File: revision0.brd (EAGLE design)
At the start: 99.5 x 80 mm, 105 parts, among them IC1 MSP430FR698X(1)80-PIN_PN, IC3 FT232RL

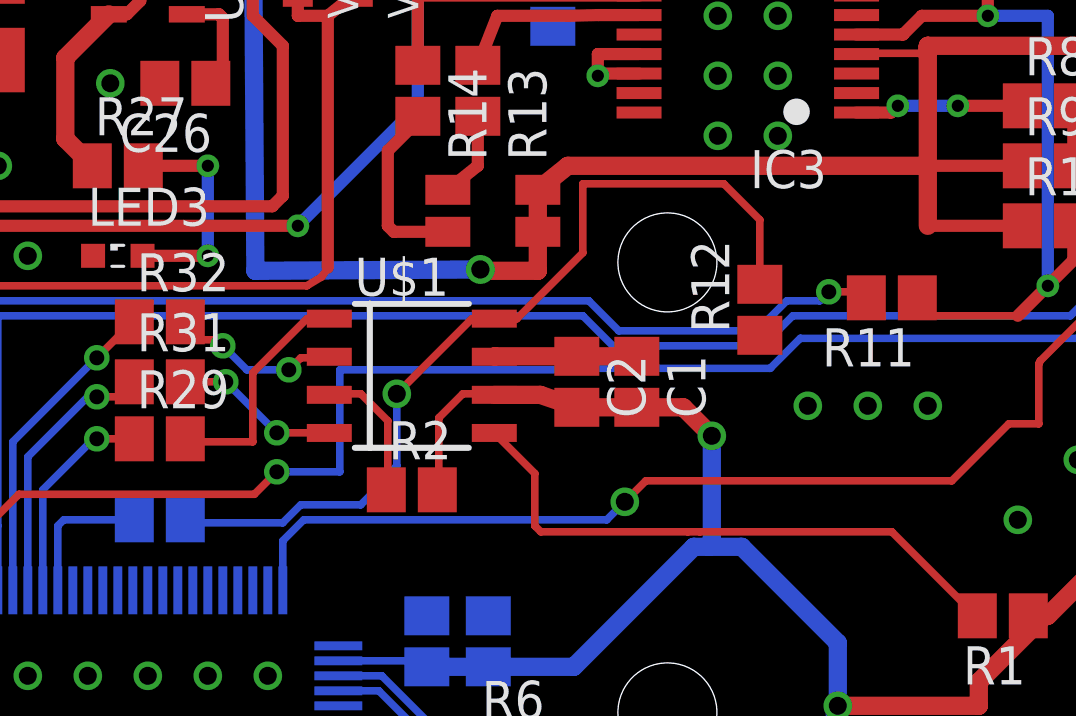
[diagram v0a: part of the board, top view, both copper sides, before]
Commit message: Fix SPI flash package foot print on PCB
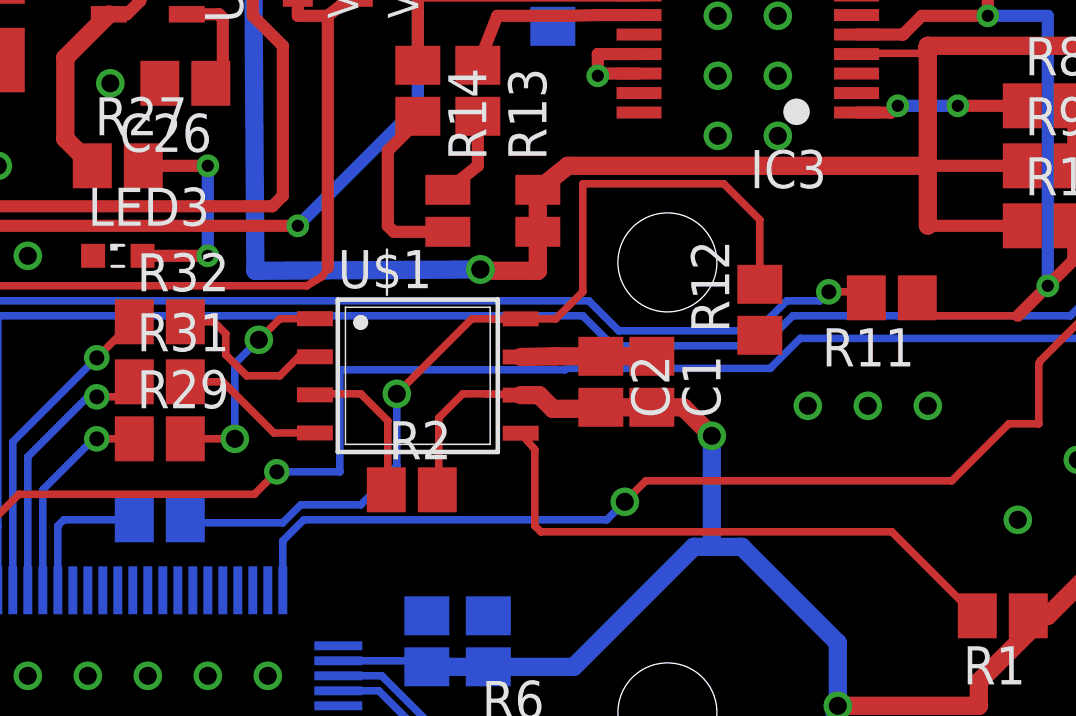
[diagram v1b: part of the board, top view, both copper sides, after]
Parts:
- U$1: value AT45DB641E-SHN -> AT45DB641E-SHNJSOP-08; device tagps:SOIC8 -> tagps:JSOP-08
- moved C2 0.80 mm to (28.1, 60.8)
- moved C1 0.50 mm to (29.8, 60.8)
- moved U$1 0.20 mm to (22.0, 61.0)
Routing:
- net N$14: track 29.5 -> 32.4 mm
- net SPICLK: track 5.93 -> 7.07 mm, vias 2 -> 0
- net SPICSN: track 5.69 -> 5.03 mm, vias 2 -> 0
- net SPISI: track 7.99 -> 7.63 mm, vias 0 -> 2

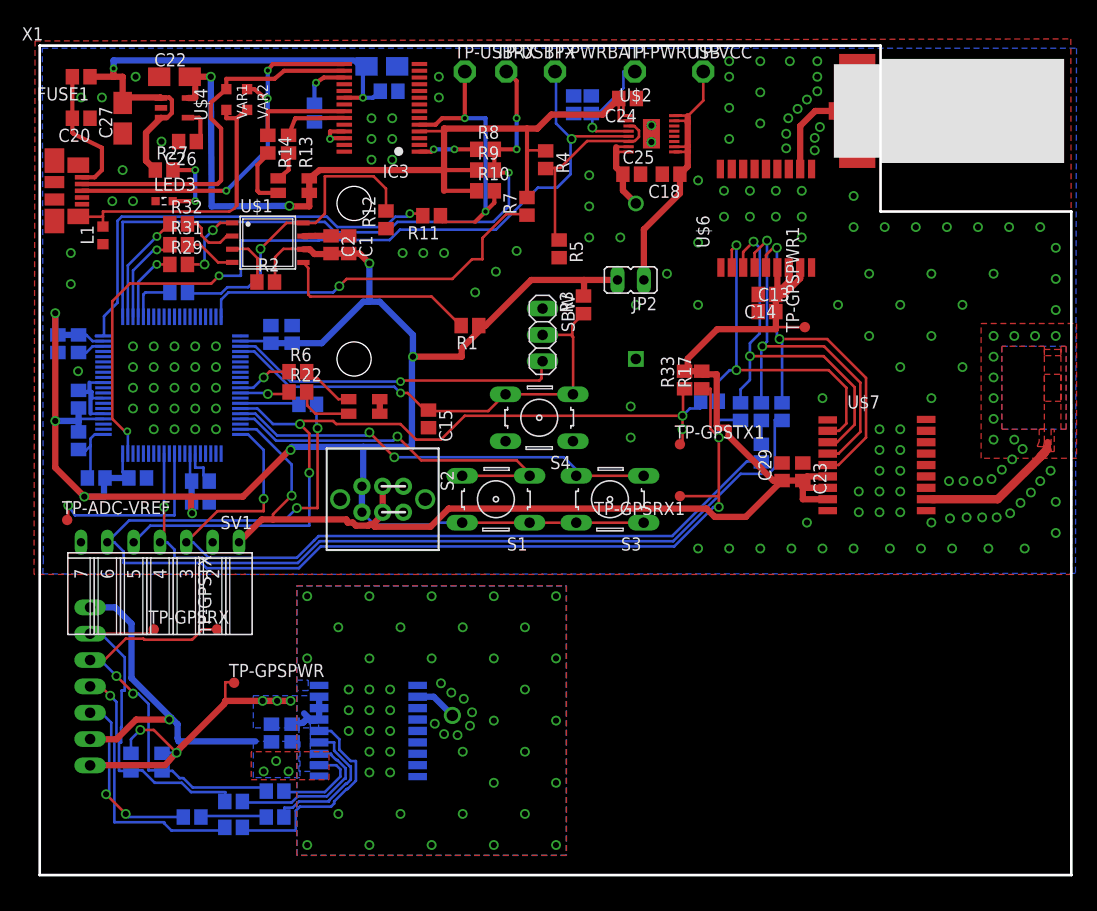
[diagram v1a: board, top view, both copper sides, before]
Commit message: Resize Cc and Rs from 0805->0603
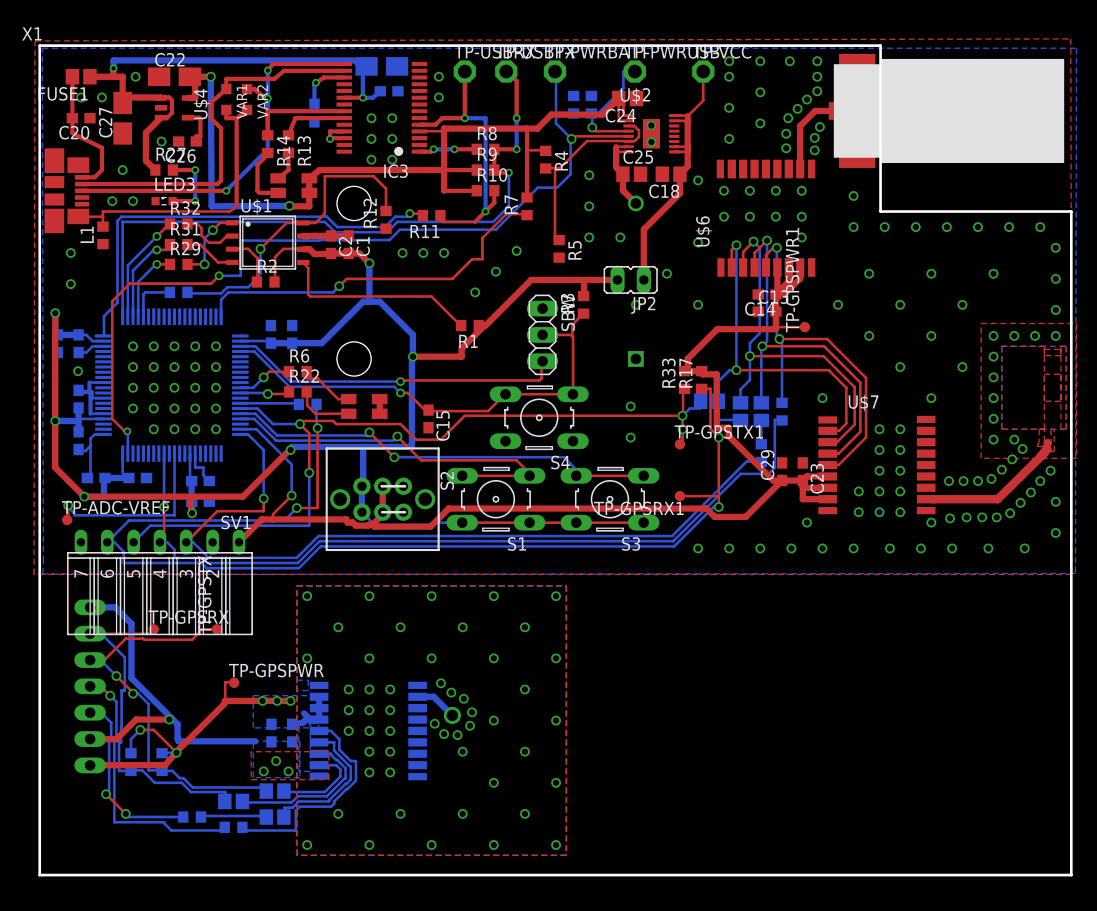
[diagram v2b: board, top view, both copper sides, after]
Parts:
- C1, C10, C11, C12, C13, C14, C15, C16, C17, C19, C2, C20, C21, C23, C26, C29, C3, C4, C5, C6, C7, C8, C9: device tagps:C0805 -> tagps:C0603
- R1, R10, R11, R12, R13, R14, R15, R16, R17, R2, R22, R23, R24, R25, R26, R27, R28, R29, R3, R30, R31, R32, R33, R34, R35, R4, R5, R6, R7, R8, R9: device tagps:R0805 -> tagps:R0603

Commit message: Split board to 2 pieces, remove ADC battery input (was senseless)
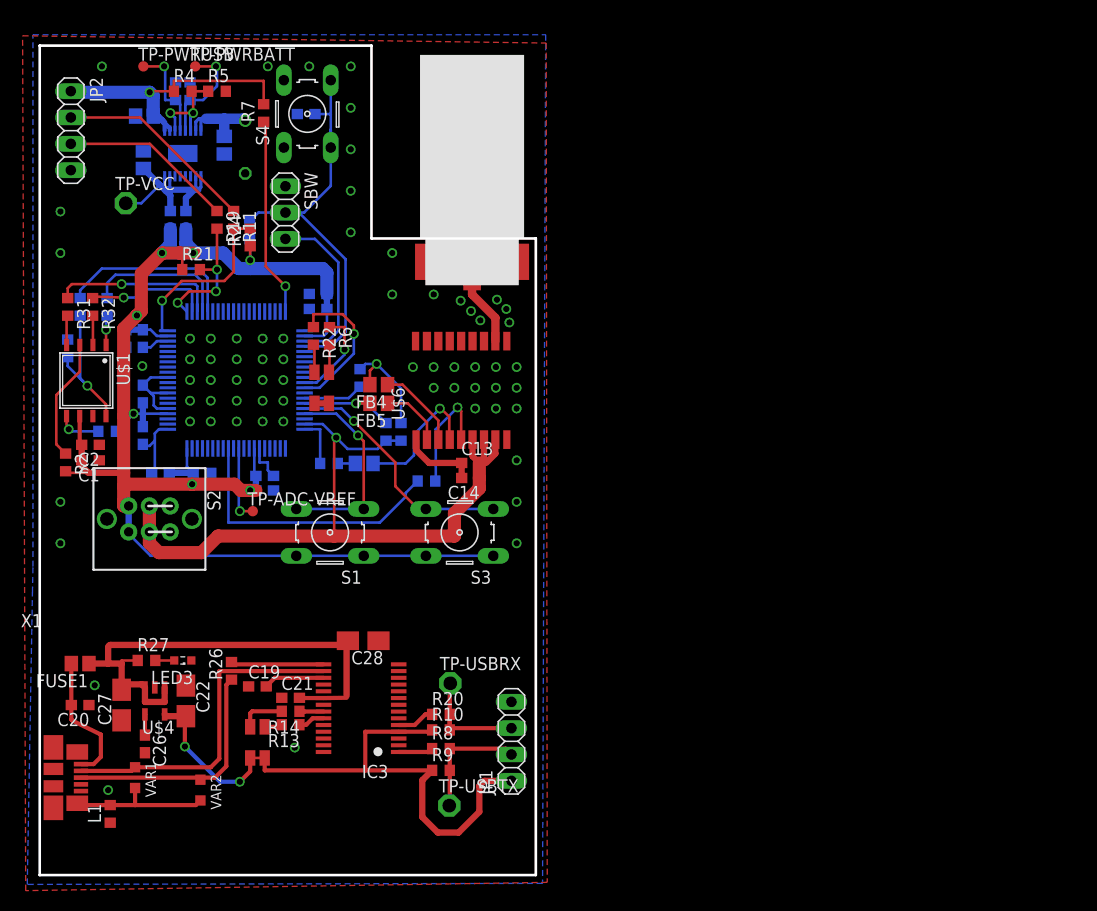
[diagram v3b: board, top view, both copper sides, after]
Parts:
- removed C16, C23: 100n, tagps:C0603
- removed C17, C29: 1u, tagps:C0603
- removed FB1, FB2, FB3: 0, tagps:R0805
- removed R28: 0, tagps:R0603
- removed SV1: (no value), tagps:FE07W
- removed TP-GPSPWR, TP-GPSPWR1, TP-GPSRX, TP-GPSRX1, TP-GPSTX, TP-GPSTX1: TPSQTP10R, tagps:TP10R
- removed TP1: TPSQTP16R, tagps:TP16R
- removed U$3, U$7: MAX-8C-0, tagps:MAX-8
- added R18: 0, tagps:R0603
- added R19, R20: 100, tagps:R0603
- added R21: 33k, tagps:R0603
- G2: value BATTERY -> BATTERYTAP5-45; device tagps:BATHOLD2AA -> tagps:TAP5-45
- JP1: device tagps:1X07/90 -> tagps:1X04
- JP2: device tagps:JP1 -> tagps:1X04
- R24: value 100k -> 33k
- R25: value 100k -> 0
- TP-PWRBATT, TP-PWRUSB: value TPSQPAD1-13 -> TPSQTP10R; device tagps:P1-13 -> tagps:TP10R
- moved TP-USBTX 71.0 mm to (39.5, 6.70)
- moved VAR2 66.8 mm to (15.5, 8.20)
- moved VAR1 66.0 mm to (9.20, 9.40)
- moved C22 60.2 mm to (14.1, 16.8), turned to 270 degrees
- moved C21 59.3 mm to (24.2, 17.1), flipped to the top
- moved TP-USBRX 59.0 mm to (39.6, 18.5)
- moved C26 58.2 mm to (10.2, 12.7), turned to 270 degrees
- moved R9 58.1 mm to (38.7, 10.1)
- moved R8 58.0 mm to (38.7, 12.2)
- moved IC3 57.9 mm to (31.0, 16.1)
- moved U$4 57.2 mm to (11.1, 16.8), turned to 180 degrees
- moved TP-VCC 57.1 mm to (8.30, 64.8)
- moved C20 56.6 mm to (3.90, 16.4)
- moved C27 56.6 mm to (7.90, 16.4)
- moved FUSE1 56.6 mm to (3.90, 20.4)
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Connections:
- removed net ANTENNA: TP1.TP, U$3.11
- removed net GPS-RX: FB1.2, JP1.2, R24.1, TP-GPSRX.TP
- removed net GPS-TIMEPULSE: JP1.5, R28.1
- removed net GPS-TX: FB2.2, JP1.3, R25.1, TP-GPSTX.TP
- removed net GPS-WAKEUP: JP1.4, R26.1
- removed net N$21: FB3.1, U$3.4
- removed net N$50: FB6.1, U$6.4, U$7.4
- removed net N$51: FB2.1, U$3.2
- removed net N$52: FB1.1, U$3.3
- removed net N$9: FB3.2, R28.2
- removed net PWR_GPS_SENSE: C16.2, C17.1, JP1.7, R24.2, R25.2, TP-GPSPWR.TP, U$3.6, U$3.7, U$3.8
- new net FT232-RX: JP1.3, R10.2, R20.2, TP-USBRX.TP
- new net FT232-TX: JP1.2, R8.2, R9.2, TP-USBTX.TP
- new net N$29: IC3.15, R26.2
- new net N$4: IC3.5, R20.1
- new net N$60: FB6.1, U$6.4
- new net VCCUSBGPS: C24.2, JP2.1, R4.1, R7.2, U$2.1, U$2.2
- net ADC-BATT: no longer IC1.59
- net GND: now also JP1.4, JP2.4; no longer C16.1, C17.2, C23.1, C29.2, JP1.1, JP1.6, SV1.2, SV1.7, U$3.1, U$3.10, U$3.12, U$7.1, U$7.10, U$7.12
- net MB-GPS-RX: no longer SV1.6, TP-GPSRX1.TP
- net MB-GPS-TIMEPULSE: no longer SV1.3
- net MB-GPS-TX: no longer SV1.5, TP-GPSTX1.TP
- net MB-GPS-WAKEUP: no longer SV1.4
- net MB-PWR_GPS_SENSE: no longer C23.2, C29.1, SV1.1, TP-GPSPWR1.TP, U$7.6, U$7.7, U$7.8
- net MCU-RX-FT232: now also R19.2, R21.2; no longer R8.2, R9.2, TP-USBTX.TP
- net MCU-TX-FT232: now also JP2.2; no longer IC3.5, R10.2, TP-USBRX.TP
- net N$12: now also R26.1; no longer IC3.15
- net N$15: no longer U$7.3
- net N$2: now also R24.2
- net N$26: now also R18.1, R25.1; no longer JP2.1
- net N$46: no longer U$7.5
- net N$49: no longer U$7.2
- net N$8: now also JP2.3, R19.1; no longer R26.2, U$3.5
- net VCC: now also R18.2, R21.1, R24.1, R25.2; no longer JP2.2
- net VCCUSB: now also JP1.1; no longer C24.2, R4.1, R7.2, U$2.1, U$2.2
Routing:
- net MB-GPS-RX: track 115.0 -> 10.7 mm, vias 4 -> 1
- net ADC-BATT: track 84.7 -> 10.2 mm, vias 3 -> 1
- net MB-GPS-TIMEPULSE: track 77.5 -> 4.80 mm, vias 1 -> 0
- net MB-GPS-TX: track 81.8 -> 9.99 mm, vias 4 -> 1
- net MB-PWR_GPS_SENSE: track 129.3 -> 70.5 mm
- net MCU-RX-FT232: track 64.9 -> 13.2 mm
- net MB-GPS-WAKEUP: track 78.5 -> 27.3 mm, vias 1 -> 0
- net GPS-TX: track 39.9 -> 0.00 mm, vias 2 -> 0
- net N$50: track 38.6 -> 0.00 mm, vias 2 -> 0
- net PWR_GPS_SENSE: track 38.3 -> 0.00 mm, vias 5 -> 0
- net GND: track 66.6 -> 30.5 mm, vias 221 -> 66
- net VCC: track 190.4 -> 155.7 mm
- net GPS-RX: track 34.2 -> 0.00 mm
- net N$15: track 37.7 -> 8.18 mm, vias 2 -> 0
- net N$49: track 35.4 -> 6.22 mm, vias 2 -> 0
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- removed copper zone on layer 1, net N$20
- removed copper zone on layer 1, net N$28
- removed copper zone on layer 16, net N$28
- removed copper zone on layer 1, net N$29
- removed copper zone on layer 1, net N$30
- removed copper zone on layer 16, net N$4
- removed copper zone on layer 16, net PWR_GPS_SENSE
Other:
- board size 99.5 x 80 mm -> 47.9 x 80 mm
- board text added: "PWRBATT"
- board text added: "PWRUSB"
- board text added: "taGPS v3a"
- board text removed: "BATT-PWR-USB"
- board text removed: "GPS-PWR"
- board text removed: "RX-GPS-TX"
- board text removed: "TIMEPULSE"
- board text removed: "taGPS v2 - antenna test"

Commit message: Remove UART pullups and button to make it even smaller
Removed GPS and USB pullups (do not forget to add them
to the MCU IOs!), removed one button, removed unnecesary
GPS ferrite beads
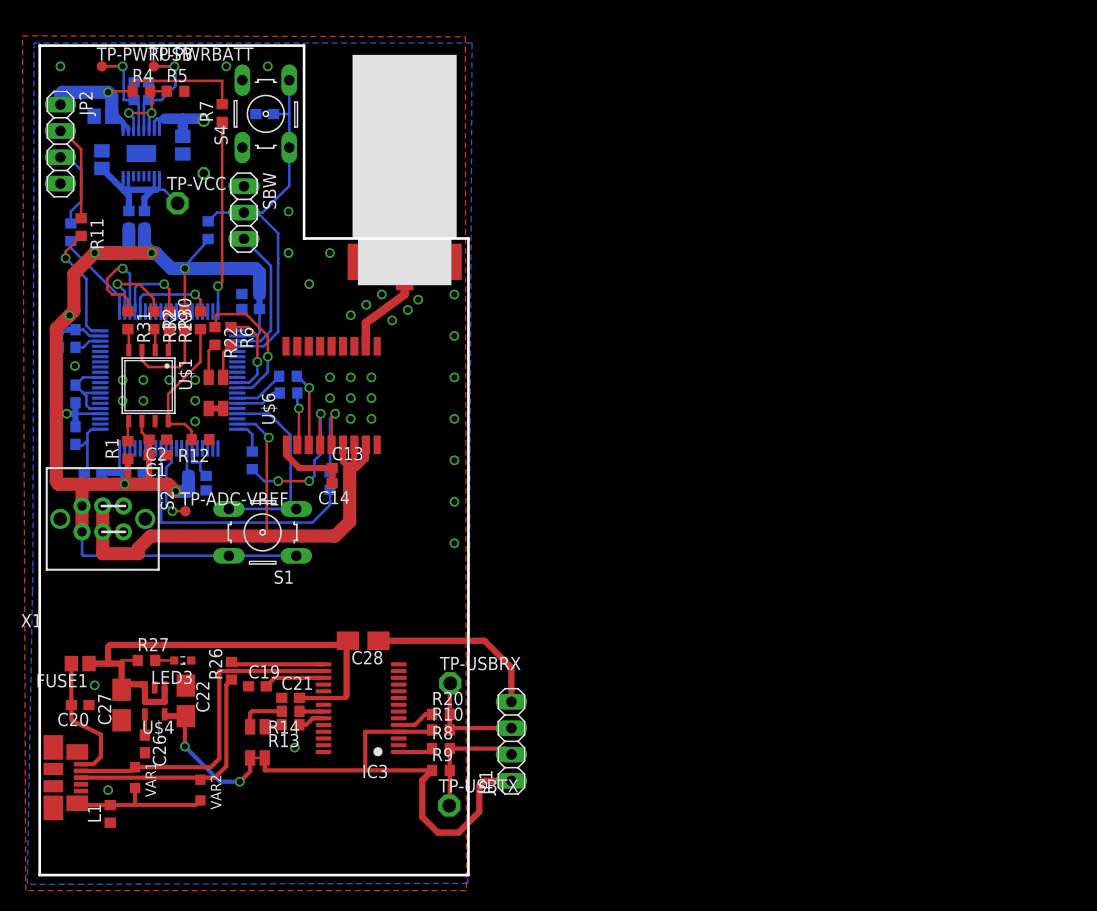
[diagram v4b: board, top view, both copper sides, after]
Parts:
- removed FB4, FB5, FB6: 0, tagps:R0805
- removed R17, R33: 100k, tagps:R0603
- removed R21, R24: 33k, tagps:R0603
- removed S3: (no value), tagps:B3F-10XX
- added R28: 100, tagps:R0603
- moved R2 17.9 mm to (14.0, 53.5), turned to 90 degrees
- moved R12 15.5 mm to (15.5, 42.0), flipped to the top, turned to 180 degrees
- moved R11 14.7 mm to (4.00, 62.5)
- moved R19 14.2 mm to (3.00, 62.0), flipped to the bottom
- moved U$6 12.5 mm to (23.1, 51.1)
- moved C13 12.5 mm to (29.1, 39.2)
- moved C14 12.5 mm to (29.1, 37.8)
- moved R30 11.7 mm to (15.5, 53.5), flipped to the top
- moved LED1 10.2 mm to (17.0, 46.5)
- moved R22 9.50 mm to (16.9, 52.0)
- moved R6 9.50 mm to (18.4, 52.0)
- moved R34 9.30 mm to (28.0, 38.0), turned to 90 degrees
- moved R35 7.41 mm to (20.5, 40.0), turned to 270 degrees
- moved R23 6.95 mm to (23.9, 48.1), turned to 180 degrees
- moved C1 6.52 mm to (11.4, 40.5)
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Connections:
- removed net N$15: FB4.1, U$6.3
- removed net N$49: FB5.1, U$6.2
- removed net N$60: FB6.1, U$6.4
- removed net SW-CHECK-BATT-MEM: IC1.36, S3.3, S3.4
- new net N$45: IC1.35, R28.1
- net MB-GPS-RX: now also U$6.3; no longer FB4.2, R17.1
- net MB-GPS-TX: now also R28.2, U$6.2; no longer FB5.2, IC1.35, R33.1
- net MB-PWR_GPS_SENSE: no longer R17.2, R33.2
- net MCU-RX-FT232: no longer R21.2
- net N$2: no longer R24.2
- net N$47: now also U$6.4; no longer FB6.2
- net VCC: no longer R21.1, R24.1, S3.1, S3.2
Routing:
- net SW-CHECK-BATT-MEM: track 23.6 -> 0.00 mm, vias 1 -> 0
- net GND: track 30.5 -> 47.7 mm, vias 66 -> 39
- net N$47: track 1.70 -> 16.0 mm, vias 0 -> 3
- net MB-PWR_GPS_SENSE: track 70.5 -> 56.5 mm
- net N$60: track 13.3 -> 0.00 mm, vias 1 -> 0
- net VCC: track 155.7 -> 144.2 mm
- net MCU-TX-FT232: track 19.4 -> 9.38 mm
- net SPISO: track 17.5 -> 8.63 mm, vias 0 -> 1
- net N$8: track 16.8 -> 8.07 mm
- net N$15: track 8.18 -> 0.00 mm
- net N$49: track 6.22 -> 0.00 mm
- net N$3: track 14.1 -> 8.13 mm, vias 0 -> 1
- net N$2: track 17.5 -> 11.7 mm
- net N$35: track 16.1 -> 11.0 mm
- net MB-GPS-TX: track 9.99 -> 5.12 mm
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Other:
- board size 47.9 x 80 mm -> 41.4 x 80 mm
- board text removed: "MEM-BATT-STAT"
